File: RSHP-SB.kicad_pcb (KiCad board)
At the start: 2 copper layers, 120 x 120 mm, 23 parts, among them J1 Conn_02x20_Odd_Even, J2 Conn_02x02_Odd_Even, J3 Conn_02x02_Odd_Even, J4 Conn_02x04_Odd_Even

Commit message: Changed mount holes to M4 diameter. Generated CAM files.
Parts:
- H12, H13, H14, H15: footprint MountingHole:MountingHole_5.3mm_M5_Pad -> MountingHole:MountingHole_4.3mm_M4_Pad
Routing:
- net EARTH: vias 29 -> 36

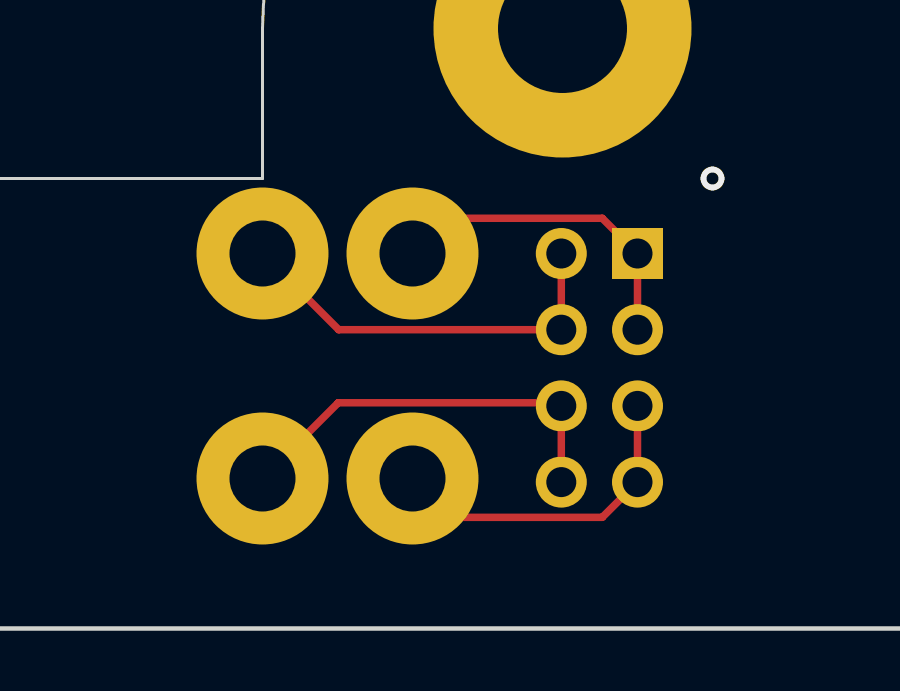
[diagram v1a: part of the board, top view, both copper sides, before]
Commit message: Made TR1 and TR2 wires thicker. Generated CAM files.
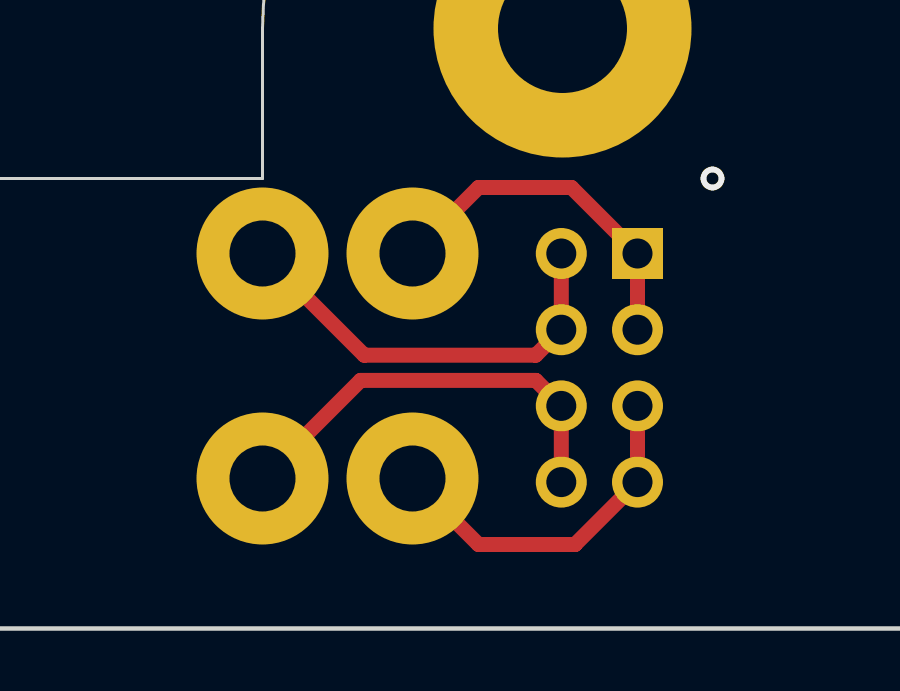
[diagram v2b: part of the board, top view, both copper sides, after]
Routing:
- net TR1_GND: track 11.6 -> 12.5 mm
- net TR2_GND: track 11.6 -> 12.4 mm
- net TR1_VCC: track 13.6 -> 14.3 mm
- net TR2_VCC: track 13.6 -> 14.2 mm
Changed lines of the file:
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@@
   (title_block
     (title "RSHP-SB-0010")
-    (date "2022-05-25")
+    (date "2022-05-29")
     (rev "1.0")
     (company "(c) Andriy Golovnya http://redscorp.net")
@@
   (via (at 145 55) (size 0.8) (drill 0.4) (layers "F.Cu" "B.Cu") (free) (net 3))
   (via (at 75 135) (size 0.8) (drill 0.4) (layers "F.Cu" "B.Cu") (free) (net 3))
-  (segment (start 149.96 140.04) (end 142.54 140.04) (width 0.25) (layer "F.Cu") (net 4))
-  (segment (start 149.96 140.04) (end 149.96 137.5) (width 0.25) (layer "F.Cu") (net 4))
-  (segment (start 142.54 140.04) (end 140 137.5) (width 0.25) (layer "F.Cu") (net 4))
-  (segment (start 151.325489 136.325489) (end 146.174511 136.325489) (width 0.25) (layer "F.Cu") (net 5))
-  (segment (start 152.5 140.04) (end 152.5 137.5) (width 0.25) (layer "F.Cu") (net 5))
-  (segment (start 152.5 137.5) (end 151.325489 136.325489) (width 0.25) (layer "F.Cu") (net 5))
-  (segment (start 146.174511 136.325489) (end 145 137.5) (width 0.25) (layer "F.Cu") (net 5))
+  (segment (start 143.39 140.89) (end 140 137.5) (width 0.5) (layer "F.Cu") (net 4))
+  (segment (start 149.96 140.04) (end 149.11 140.89) (width 0.5) (layer "F.Cu") (net 4))
+  (segment (start 149.96 140.04) (end 149.96 137.5) (width 0.5) (layer "F.Cu") (net 4))
+  (segment (start 149.11 140.89) (end 143.39 140.89) (width 0.5) (layer "F.Cu") (net 4))
+  (segment (start 150.300001 135.300001) (end 152.5 137.5) (width 0.5) (layer "F.Cu") (net 5))
+  (segment (start 147.199999 135.300001) (end 150.300001 135.300001) (width 0.5) (layer "F.Cu") (net 5))
+  (segment (start 145 137.5) (end 147.199999 135.300001) (width 0.5) (layer "F.Cu") (net 5))
   (segment (start 152.5 137.5) (end 153.135718 137.5) (width 0.25) (layer "F.Cu") (net 5))
-  (segment (start 149.96 145.12) (end 149.96 142.58) (width 0.25) (layer "F.Cu") (net 6))
-  (segment (start 149.855489 142.475489) (end 142.524511 142.475489) (width 0.25) (layer "F.Cu") (net 6))
-  (segment (start 142.524511 142.475489) (end 140 145) (width 0.25) (layer "F.Cu") (net 6))
-  (segment (start 149.96 142.58) (end 149.855489 142.475489) (width 0.25) (layer "F.Cu") (net 6))
-  (segment (start 146.294511 146.294511) (end 145 145) (width 0.25) (layer "F.Cu") (net 7))
+  (segment (start 152.5 140.04) (end 152.5 137.5) (width 0.5) (layer "F.Cu") (net 5))
+  (segment (start 143.27 141.73) (end 140 145) (width 0.5) (layer "F.Cu") (net 6))
+  (segment (start 149.96 145.12) (end 149.96 142.58) (width 0.5) (layer "F.Cu") (net 6))
+  (segment (start 149.11 141.73) (end 143.27 141.73) (width 0.5) (layer "F.Cu") (net 6))
+  (segment (start 149.96 142.58) (end 149.11 141.73) (width 0.5) (layer "F.Cu") (net 6))
+  (segment (start 147.199999 147.199999) (end 145 145) (width 0.5) (layer "F.Cu") (net 7))
+  (segment (start 152.5 145.12) (end 150.420001 147.199999) (width 0.5) (layer "F.Cu") (net 7))
   (segment (start 152.5 142.58) (end 153.055718 142.58) (width 0.25) (layer "F.Cu") (net 7))
-  (segment (start 151.325489 146.294511) (end 146.294511 146.294511) (width 0.25) (layer "F.Cu") (net 7))
-  (segment (start 152.5 145.12) (end 151.325489 146.294511) (width 0.25) (layer "F.Cu") (net 7))
-  (segment (start 152.5 145.12) (end 152.5 142.58) (width 0.25) (layer "F.Cu") (net 7))
+  (segment (start 150.420001 147.199999) (end 147.199999 147.199999) (width 0.5) (layer "F.Cu") (net 7))
+  (segment (start 152.5 145.12) (end 152.5 142.58) (width 0.5) (layer "F.Cu") (net 7))
   (zone (net 1) (net_name "HE_VCC") (layers F&B.Cu) (hatch edge 0.508)
     (priority 1)
